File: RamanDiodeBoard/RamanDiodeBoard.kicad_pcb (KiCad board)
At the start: 2 copper layers, 38.1 x 38.1 mm, 14 parts, among them Q1 BSS138, Q2 BSS138

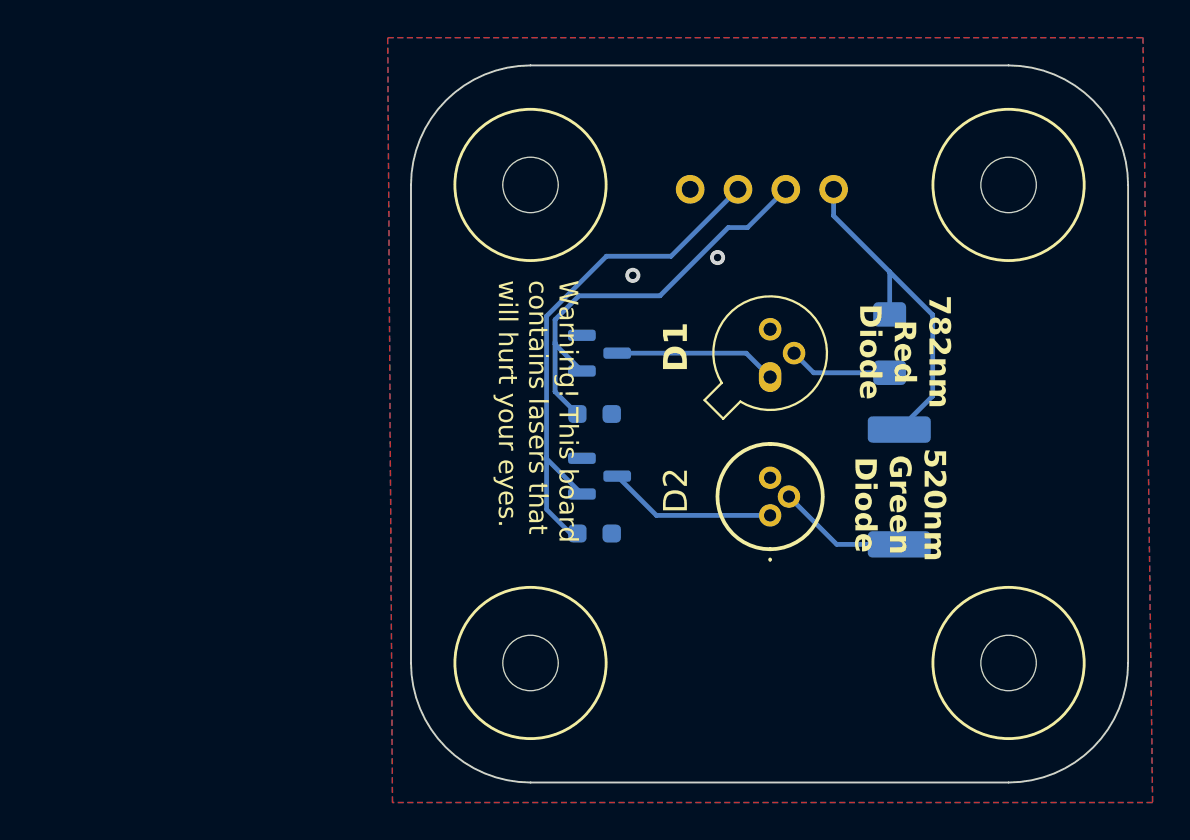
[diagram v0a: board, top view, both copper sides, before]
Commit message: laser diode board changes
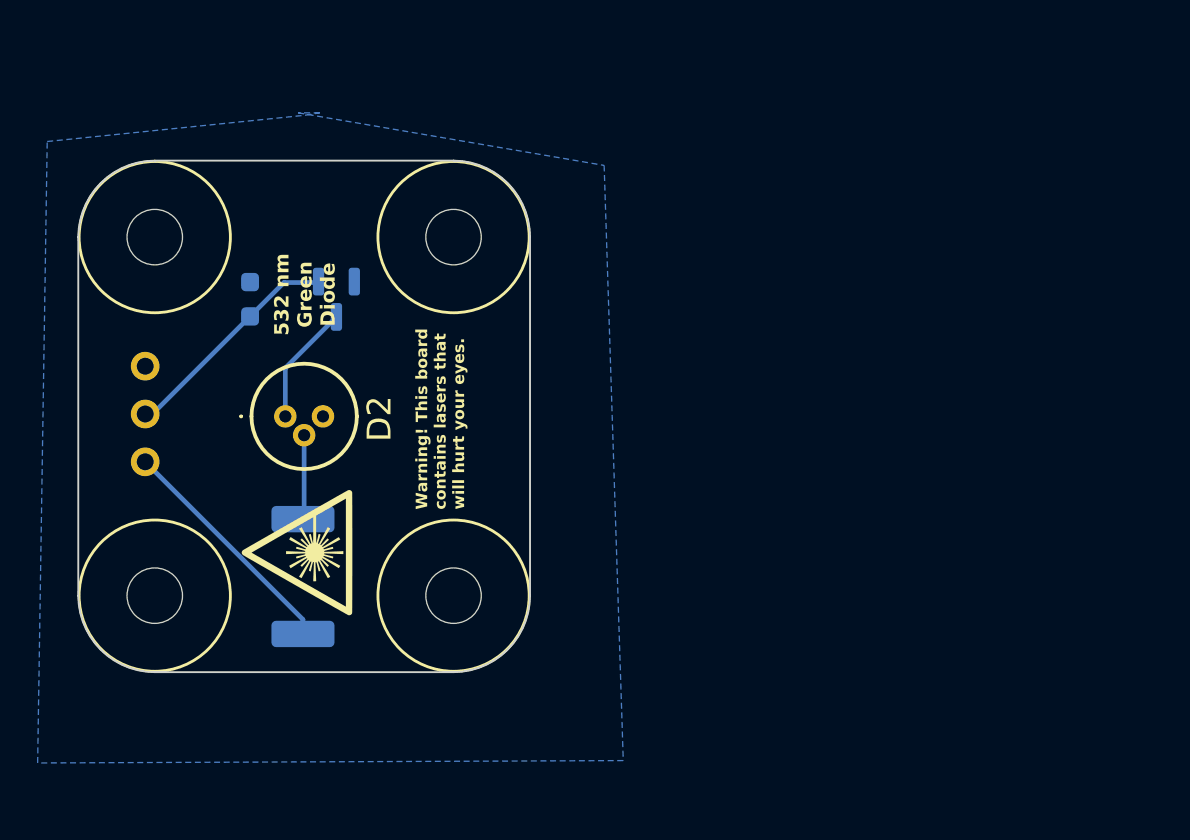
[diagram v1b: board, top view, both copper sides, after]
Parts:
- removed Conn1: Molex_SL_04, MRDT_Connectors:MOLEX_SL_04_Vertical
- removed D1: 782nm Laser Diode, Package_TO_SOT_THT:TO-18-3
- removed Q2: BSS138, Package_TO_SOT_SMD:SOT-23
- removed R2: 78.7, Resistor_SMD:R_1206_3216Metric_Pad1.30x1.75mm_HandSolder
- removed R4: 4.7k, Resistor_SMD:R_0603_1608Metric_Pad0.98x0.95mm_HandSolder
- added Conn2: Molex_SL_03, MRDT_Connectors:MOLEX_SL_03_Vertical, B.Cu at (33.8, 36.8)
- added G***: LOGO, LOGO, F.Cu at (41.9, 41.7)
- moved V4 45.5 mm to (34.3, 43.9)
- moved V1 45.4 mm to (34.3, 24.9)
- moved R1 32.0 mm to (42.2, 42.9), turned to 90 degrees
- moved D2 26.3 mm to (41.2, 34.4), turned to 0 degrees
- moved V2 23.0 mm to (50.2, 24.9)
- moved V3 22.2 mm to (50.2, 43.9)
- moved R3 22.1 mm to (39.4, 28.2), turned to 90 degrees
- moved Q1 16.8 mm to (43.9, 28.2), turned to -90 degrees
- moved G*** 16.8 mm to (68.3, 24.6), turned to 0 degrees
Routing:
- net Red_LED: track 22.7 -> 0.00 mm
- net Green_LED: track 28.1 -> 12.1 mm
- net Net-(D1-K): track 8.65 -> 0.00 mm
- net Net-(D1-A): track 5.51 -> 0.00 mm
- net +12V: track 17.9 -> 12.6 mm
- net Net-(D2-K): track 8.99 -> 6.41 mm
- net Net-(D2-A): track 6.91 -> 4.49 mm
- net GND: vias 2 -> 0
- removed copper zone on F.Cu, net GND
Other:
- board size 38.1 x 38.1 mm -> 24 x 27.2 mm
- board text added: "532 nm Green Diode"
- board text added: "Raman Diode Breakout, Rev2 Mars Rover Design Team Missouri S&T, 2024 Caleb Ehlers"
- board text removed: "520nm Green Diode"
- board text removed: "782nm Red Diode"
- board text removed: "Diode Breakout, Rev1 Mars Rover Design Team Missouri S&T, 2024 Caleb Ehlers"

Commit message: misc cleanup
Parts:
- removed the G*** at (68.3, 24.6)
